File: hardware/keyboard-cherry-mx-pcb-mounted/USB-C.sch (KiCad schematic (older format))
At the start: 3 parts

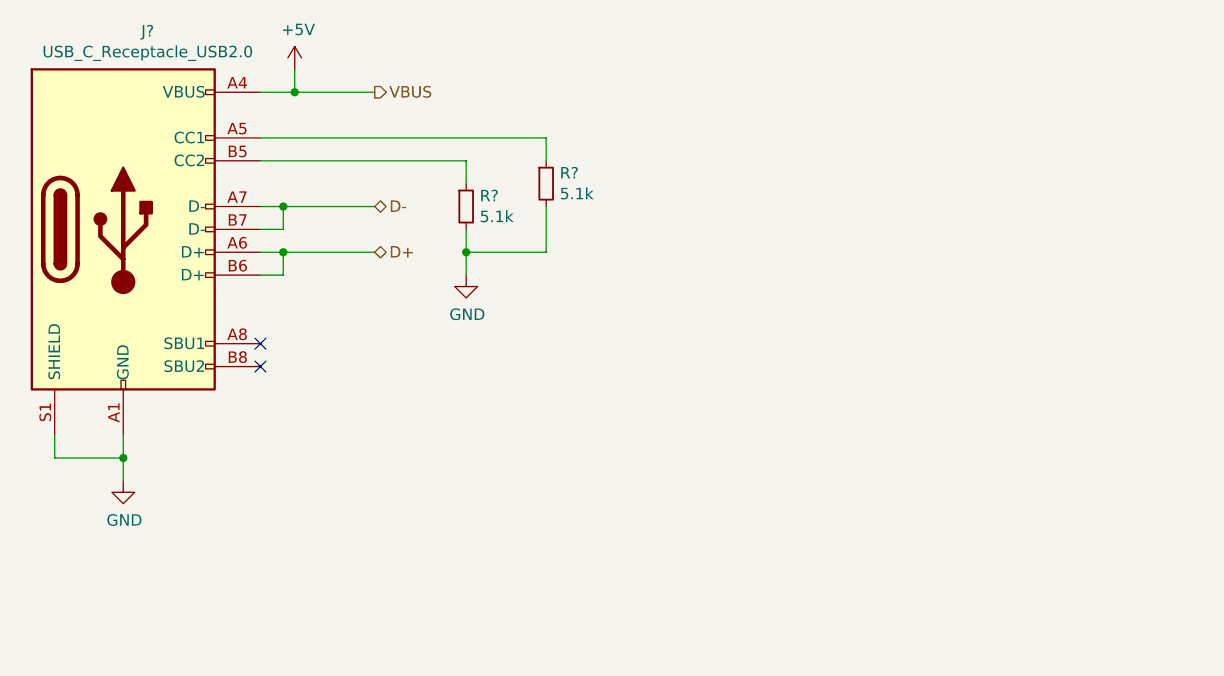
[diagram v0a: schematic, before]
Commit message: Adds completed sensor and power connections. Still need to add USB footprint then sch are done for version 1.0
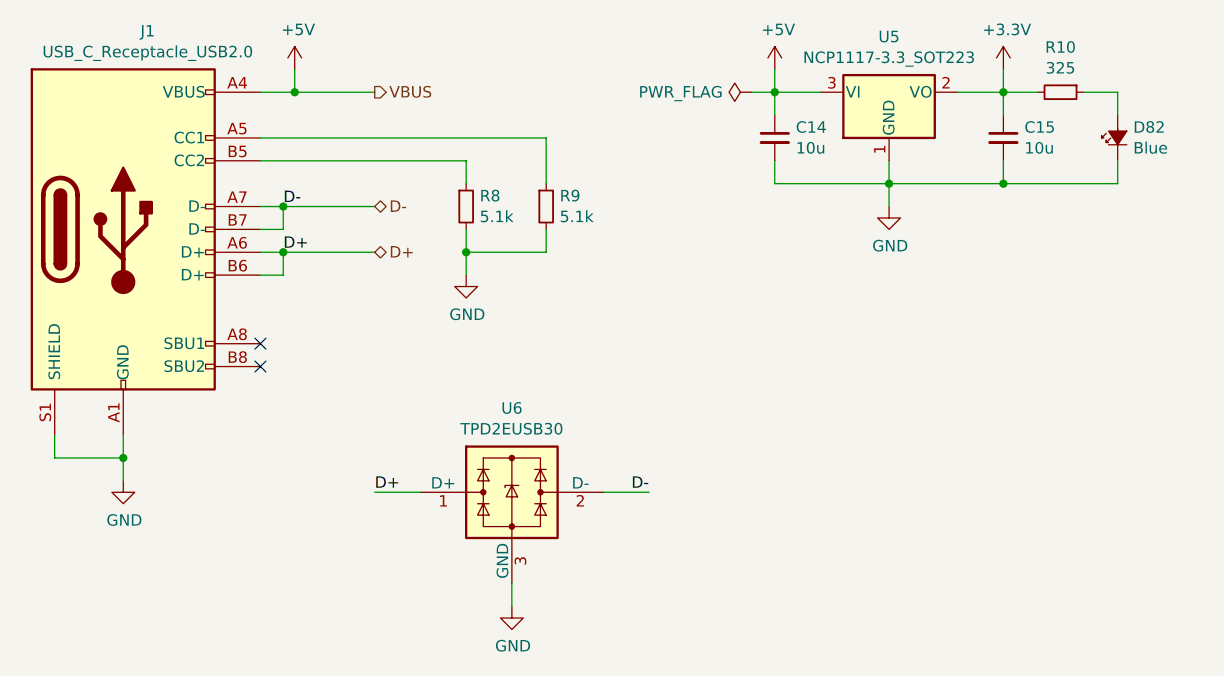
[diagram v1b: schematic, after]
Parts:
- added C14, C15: 10u, Capacitor_SMD:C_0805_2012Metric, symbol Device:C_Small
- added D82: Blue, symbol Device:LED_Small_ALT
- added R10: 325, symbol Device:R_Small
- added U5: NCP1117-3.3_SOT223, Package_TO_SOT_SMD:SOT-223-3_TabPin2, symbol Regulator_Linear:NCP1117-3.3_SOT223
- added U6: TPD2EUSB30, Package_TO_SOT_SMD:Texas_DRT-3, symbol Power_Protection:TPD2EUSB30
- gave numbers to parts that had none: 3
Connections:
- net +5V: now also C14.1, U5.3 (VI)
- net D+: now also U6.1 (D+)
- net D-: now also U6.2 (D-)
- net GND: now also C14.2, C15.2, D82.1 (K), U5.1 (GND), U6.3 (GND)
- new net: D82.2 (A), R10.1
- new net +3V3: C15.1, R10.2, U5.2 (VO)
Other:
- moved on the sheet: R9
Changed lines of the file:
@@
 $EndDescr
 $Comp
-L Connector:USB_C_Receptacle_USB2.0 J?
+L Connector:USB_C_Receptacle_USB2.0 J1
 U 1 1 5E8055B4
 P 2400 3250
-F 0 "J?" H 2507 4117 50  0000 C CNN
+F 0 "J1" H 2507 4117 50  0000 C CNN
 F 1 "USB_C_Receptacle_USB2.0" H 2507 4026 50  0000 C CNN
 F 2 "" H 2550 3250 50  0001 C CNN
@@
 D+
 $Comp
-L Device:R_Small R?
+L Device:R_Small R9
 U 1 1 5E80893D
-P 4250 3050
-F 0 "R?" H 4309 3096 50  0000 L CNN
-F 1 "5.1k" H 4309 3005 50  0000 L CNN
-F 2 "Resistor_SMD:R_0805_2012Metric" H 4250 3050 50  0001 C CNN
-F 3 "~" H 4250 3050 50  0001 C CNN
-	1    4250 3050
-	1    0    0    -1
-$EndComp
-$Comp
-L Device:R_Small R?
+P 4250 3150
+F 0 "R9" H 4309 3196 50  0000 L CNN
+F 1 "5.1k" H 4309 3105 50  0000 L CNN
+F 2 "Resistor_SMD:R_0805_2012Metric" H 4250 3150 50  0001 C CNN
+F 3 "~" H 4250 3150 50  0001 C CNN
+	1    4250 3150
+	1    0    0    -1
+$EndComp
+$Comp
+L Device:R_Small R8
 U 1 1 5E80B2F7
 P 3900 3150
-F 0 "R?" H 3959 3196 50  0000 L CNN
+F 0 "R8" H 3959 3196 50  0000 L CNN
 F 1 "5.1k" H 3959 3105 50  0000 L CNN
 F 2 "Resistor_SMD:R_0805_2012Metric" H 3900 3150 50  0001 C CNN
@@
 	3000 2850 4250 2850
 Wire Wire Line
-	4250 2850 4250 2950
-$Comp
-L power:GND #PWR?
+	4250 2850 4250 3050
+$Comp
+L power:GND #PWR023
 U 1 1 5E80BFE4
 P 3900 3450
-F 0 "#PWR?" H 3900 3200 50  0001 C CNN
+F 0 "#PWR023" H 3900 3200 50  0001 C CNN
 F 1 "GND" H 3905 3277 50  0000 C CNN
 F 2 "" H 3900 3450 50  0001 C CNN
@@
 Connection ~ 3900 3350
 Wire Wire Line
-	4250 3150 4250 3350
+	4250 3250 4250 3350
 Wire Wire Line
 	3900 3250 3900 3350
 $Comp
-L power:GND #PWR?
+L power:GND #PWR021
 U 1 1 5E80F482
 P 2400 4350
-F 0 "#PWR?" H 2400 4100 50  0001 C CNN
+F 0 "#PWR021" H 2400 4100 50  0001 C CNN
 F 1 "GND" H 2405 4177 50  0000 C CNN
 F 2 "" H 2400 4350 50  0001 C CNN
@@
 	2400 4250 2400 4150
 $Comp
-L power:+5V #PWR?
+L power:+5V #PWR022
 U 1 1 5E810FCD
 P 3150 2550
-F 0 "#PWR?" H 3150 2400 50  0001 C CNN
+F 0 "#PWR022" H 3150 2400 50  0001 C CNN
 F 1 "+5V" H 3165 2723 50  0000 C CNN
 F 2 "" H 3150 2550 50  0001 C CNN
@@
 NoConn ~ 3000 3750
 NoConn ~ 3000 3850
+$Comp
+L Regulator_Linear:NCP1117-3.3_SOT223 U5
+U 1 1 5EA493A5
+P 5750 2650
+F 0 "U5" H 5750 2892 50  0000 C CNN
+F 1 "NCP1117-3.3_SOT223" H 5750 2801 50  0000 C CNN
+F 2 "Package_TO_SOT_SMD:SOT-223-3_TabPin2" H 5750 2850 50  0001 C CNN
+F 3 "http://www.onsemi.com/pub_link/Collateral/NCP1117-D.PDF" H 5850 2400 50  0001 C CNN
+	1    5750 2650
+	1    0    0    -1
+$EndComp
+$Comp
+L Device:C_Small C15
+U 1 1 5EA4AE93
+P 6250 2850
+F 0 "C15" H 6342 2896 50  0000 L CNN
+F 1 "10u" H 6342 2805 50  0000 L CNN
+F 2 "Capacitor_SMD:C_0805_2012Metric" H 6250 2850 50  0001 C CNN
+F 3 "~" H 6250 2850 50  0001 C CNN
+	1    6250 2850
+	1    0    0    -1
+$EndComp
+$Comp
+L Device:C_Small C14
+U 1 1 5EA4B77C
+P 5250 2850
+F 0 "C14" H 5342 2896 50  0000 L CNN
+F 1 "10u" H 5342 2805 50  0000 L CNN
+F 2 "Capacitor_SMD:C_0805_2012Metric" H 5250 2850 50  0001 C CNN
+F 3 "~" H 5250 2850 50  0001 C CNN
+	1    5250 2850
+	1    0    0    -1
+$EndComp
+Wire Wire Line
+	6250 2650 6250 2750
+Wire Wire Line
+	6250 2950 6250 3050
+Wire Wire Line
+	5250 3050 5250 2950
+Wire Wire Line
+	5750 2950 5750 3050
+Connection ~ 5750 3050
+$Comp
+L power:GND #PWR0101
+U 1 1 5EA4DBB7
+P 5750 3150
+F 0 "#PWR0101" H 5750 2900 50  0001 C CNN
+F 1 "GND" H 5755 2977 50  0000 C CNN
+F 2 "" H 5750 3150 50  0001 C CNN
+F 3 "" H 5750 3150 50  0001 C CNN
+	1    5750 3150
+	1    0    0    -1
+$EndComp
+Wire Wire Line
+	5750 3150 5750 3050
+Wire Wire Line
+	5250 2550 5250 2650
+Wire Wire Line
+	5250 2650 5450 2650
+Connection ~ 5250 2650
+Wire Wire Line
+	5250 2650 5250 2750
+Wire Wire Line
+	5250 3050 5750 3050
+Wire Wire Line
+	5750 3050 6250 3050
+$Comp
+L power:+3.3V #PWR0103
+U 1 1 5EA55914
+P 6250 2550
+F 0 "#PWR0103" H 6250 2400 50  0001 C CNN
+F 1 "+3.3V" H 6265 2723 50  0000 C CNN
+F 2 "" H 6250 2550 50  0001 C CNN
+F 3 "" H 6250 2550 50  0001 C CNN
+	1    6250 2550
+	1    0    0    -1
+$EndComp
+Wire Wire Line
+	6250 2550 6250 2650
+Connection ~ 6250 2650
+$Comp
+L Device:R_Small R10
+U 1 1 5EA56F50
+P 6500 2650
+F 0 "R10" V 6304 2650 50  0000 C CNN
+F 1 "325" V 6395 2650 50  0000 C CNN
+F 2 "" H 6500 2650 50  0001 C CNN
+F 3 "~" H 6500 2650 50  0001 C CNN
+	1    6500 2650
+	0    1    1    0
+$EndComp
+$Comp
+L Device:LED_Small_ALT D82
+U 1 1 5EA59D3F
+P 6750 2850
+F 0 "D82" V 6796 2782 50  0000 R CNN
+F 1 "Blue" V 6705 2782 50  0000 R CNN
+F 2 "" V 6750 2850 50  0001 C CNN
+F 3 "~" V 6750 2850 50  0001 C CNN
+F 4 "APTD2012LQBC/D" V 6750 2850 50  0001 C CNN "P/N"
+F 5 "2.65V" V 6750 2850 50  0001 C CNN "Vf"
+F 6 "2mA" V 6750 2850 50  0001 C CNN "If"
+	1    6750 2850
+	0    -1   -1   0
+$EndComp
+Wire Wire Line
+	6400 2650 6250 2650
+Wire Wire Line
+	6250 3050 6750 3050
+Wire Wire Line
+	6750 3050 6750 2950
+Connection ~ 6250 3050
+Wire Wire Line
+	6750 2750 6750 2650
+Wire Wire Line
+	6750 2650 6600 2650
+Wire Wire Line
+	6050 2650 6250 2650
+$Comp
+L power:+5V #PWR0102
+U 1 1 5EB4F139
+P 5250 2550
+F 0 "#PWR0102" H 5250 2400 50  0001 C CNN
+F 1 "+5V" H 5265 2723 50  0000 C CNN
+F 2 "" H 5250 2550 50  0001 C CNN
+F 3 "" H 5250 2550 50  0001 C CNN
+	1    5250 2550
+	1    0    0    -1
+$EndComp
+$Comp
+L power:PWR_FLAG #FLG0101
+U 1 1 5EB50AC0
+P 5150 2650
+F 0 "#FLG0101" H 5150 2725 50  0001 C CNN
+F 1 "PWR_FLAG" V 5150 2777 50  0000 L CNN
+F 2 "" H 5150 2650 50  0001 C CNN
+F 3 "~" H 5150 2650 50  0001 C CNN
+	1    5150 2650
+	0    -1   -1   0
+$EndComp
+Wire Wire Line
+	5150 2650 5250 2650
+$Comp
+L Power_Protection:TPD2EUSB30 U6
+U 1 1 5EB6D136
+P 4100 4400
+F 0 "U6" H 4100 4767 50  0000 C CNN
+F 1 "TPD2EUSB30" H 4100 4676 50  0000 C CNN
+F 2 "Package_TO_SOT_SMD:Texas_DRT-3" H 3350 4100 50  0001 C CNN
+F 3 "http://www.ti.com/lit/ds/symlink/tpd2eusb30a.pdf" H 4100 4400 50  0001 C CNN
+	1    4100 4400
+	1    0    0    -1
+$EndComp
+Text Label 3100 3150 0    50   ~ 0
+D-
+Text Label 3100 3350 0    50   ~ 0
+D+
+$Comp
+L power:GND #PWR024
+U 1 1 5EB72B3A
+P 4100 4900
+F 0 "#PWR024" H 4100 4650 50  0001 C CNN
+F 1 "GND" H 4105 4727 50  0000 C CNN
+F 2 "" H 4100 4900 50  0001 C CNN
+F 3 "" H 4100 4900 50  0001 C CNN
+	1    4100 4900
+	1    0    0    -1
+$EndComp
+Wire Wire Line
+	4100 4900 4100 4800
+Text Label 4700 4400 2    50   ~ 0
+D-
+Wire Wire Line
+	4700 4400 4500 4400
+Wire Wire Line
+	3700 4400 3500 4400
+Text Label 3500 4400 0    50   ~ 0
+D+
 $EndSCHEMATC

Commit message: All keys except for function key row are laid out to their exact locations.
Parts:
- D82: footprint (none) -> LED_SMD:LED_0805_2012Metric
- J1: footprint (none) -> Sij_Connectors:USB_C_Receptacle_Wurth_632723100021; P/N (none) -> 632723100021
- R10: footprint (none) -> Resistor_SMD:R_0805_2012Metric
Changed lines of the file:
@@
 F 0 "J1" H 2507 4117 50  0000 C CNN
 F 1 "USB_C_Receptacle_USB2.0" H 2507 4026 50  0000 C CNN
-F 2 "" H 2550 3250 50  0001 C CNN
+F 2 "Sij_Connectors:USB_C_Receptacle_Wurth_632723100021" H 2550 3250 50  0001 C CNN
 F 3 "https://www.usb.org/sites/default/files/documents/usb_type-c.zip" H 2550 3250 50  0001 C CNN
+F 4 "632723100021" H 2400 3250 50  0001 C CNN "P/N"
 	1    2400 3250
 	1    0    0    -1
@@
 F 0 "R10" V 6304 2650 50  0000 C CNN
 F 1 "325" V 6395 2650 50  0000 C CNN
-F 2 "" H 6500 2650 50  0001 C CNN
+F 2 "Resistor_SMD:R_0805_2012Metric" H 6500 2650 50  0001 C CNN
 F 3 "~" H 6500 2650 50  0001 C CNN
 	1    6500 2650
@@
 F 0 "D82" V 6796 2782 50  0000 R CNN
 F 1 "Blue" V 6705 2782 50  0000 R CNN
-F 2 "" V 6750 2850 50  0001 C CNN
+F 2 "LED_SMD:LED_0805_2012Metric" V 6750 2850 50  0001 C CNN
 F 3 "~" V 6750 2850 50  0001 C CNN
 F 4 "APTD2012LQBC/D" V 6750 2850 50  0001 C CNN "P/N"

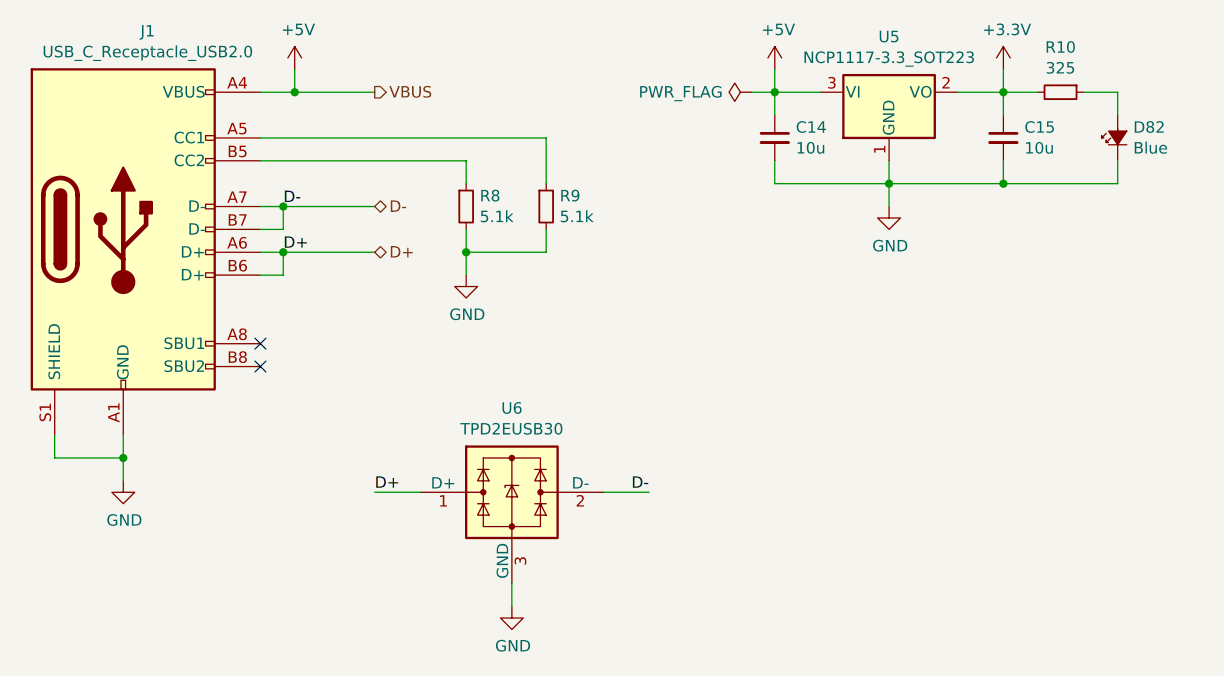
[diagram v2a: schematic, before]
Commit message: Aligns the keys so the column connections are more consistent. e.g. right most keys will have same column connection.
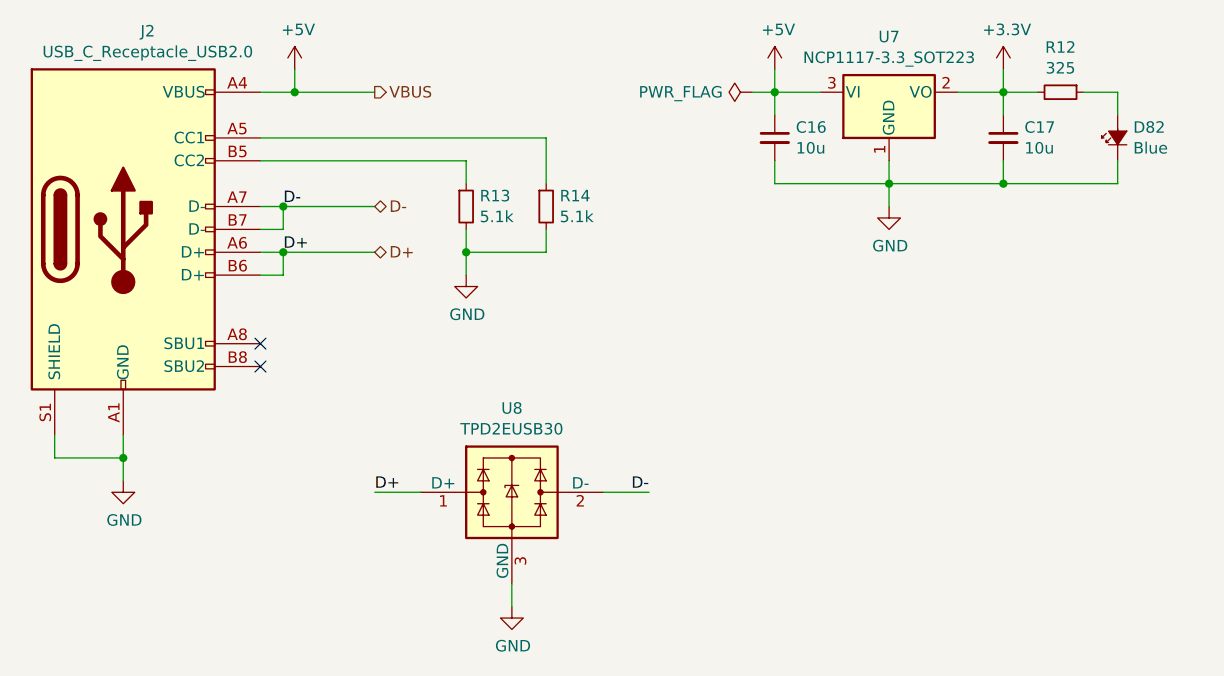
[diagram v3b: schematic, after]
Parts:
- renumbered C14 to C16, C15 to C17, J1 to J2, R10 to R12, R8 to R13, R9 to R14, U5 to U7, U6 to U8
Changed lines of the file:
@@
 $EndDescr
 $Comp
-L Connector:USB_C_Receptacle_USB2.0 J1
+L Connector:USB_C_Receptacle_USB2.0 J2
 U 1 1 5E8055B4
 P 2400 3250
-F 0 "J1" H 2507 4117 50  0000 C CNN
+F 0 "J2" H 2507 4117 50  0000 C CNN
 F 1 "USB_C_Receptacle_USB2.0" H 2507 4026 50  0000 C CNN
 F 2 "Sij_Connectors:USB_C_Receptacle_Wurth_632723100021" H 2550 3250 50  0001 C CNN
@@
 D+
 $Comp
-L Device:R_Small R9
+L Device:R_Small R14
 U 1 1 5E80893D
 P 4250 3150
-F 0 "R9" H 4309 3196 50  0000 L CNN
+F 0 "R14" H 4309 3196 50  0000 L CNN
 F 1 "5.1k" H 4309 3105 50  0000 L CNN
 F 2 "Resistor_SMD:R_0805_2012Metric" H 4250 3150 50  0001 C CNN
@@
 $EndComp
 $Comp
-L Device:R_Small R8
+L Device:R_Small R13
 U 1 1 5E80B2F7
 P 3900 3150
-F 0 "R8" H 3959 3196 50  0000 L CNN
+F 0 "R13" H 3959 3196 50  0000 L CNN
 F 1 "5.1k" H 3959 3105 50  0000 L CNN
 F 2 "Resistor_SMD:R_0805_2012Metric" H 3900 3150 50  0001 C CNN
@@
 	4250 2850 4250 3050
 $Comp
-L power:GND #PWR023
+L power:GND #PWR033
 U 1 1 5E80BFE4
 P 3900 3450
-F 0 "#PWR023" H 3900 3200 50  0001 C CNN
+F 0 "#PWR033" H 3900 3200 50  0001 C CNN
 F 1 "GND" H 3905 3277 50  0000 C CNN
 F 2 "" H 3900 3450 50  0001 C CNN
@@
 	3900 3250 3900 3350
 $Comp
-L power:GND #PWR021
+L power:GND #PWR034
 U 1 1 5E80F482
 P 2400 4350
-F 0 "#PWR021" H 2400 4100 50  0001 C CNN
+F 0 "#PWR034" H 2400 4100 50  0001 C CNN
 F 1 "GND" H 2405 4177 50  0000 C CNN
 F 2 "" H 2400 4350 50  0001 C CNN
@@
 	2400 4250 2400 4150
 $Comp
-L power:+5V #PWR022
+L power:+5V #PWR029
 U 1 1 5E810FCD
 P 3150 2550
-F 0 "#PWR022" H 3150 2400 50  0001 C CNN
+F 0 "#PWR029" H 3150 2400 50  0001 C CNN
 F 1 "+5V" H 3165 2723 50  0000 C CNN
 F 2 "" H 3150 2550 50  0001 C CNN
@@
 NoConn ~ 3000 3850
 $Comp
-L Regulator_Linear:NCP1117-3.3_SOT223 U5
+L Regulator_Linear:NCP1117-3.3_SOT223 U7
 U 1 1 5EA493A5
 P 5750 2650
-F 0 "U5" H 5750 2892 50  0000 C CNN
+F 0 "U7" H 5750 2892 50  0000 C CNN
 F 1 "NCP1117-3.3_SOT223" H 5750 2801 50  0000 C CNN
 F 2 "Package_TO_SOT_SMD:SOT-223-3_TabPin2" H 5750 2850 50  0001 C CNN
@@
 $EndComp
 $Comp
-L Device:C_Small C15
+L Device:C_Small C17
 U 1 1 5EA4AE93
 P 6250 2850
-F 0 "C15" H 6342 2896 50  0000 L CNN
+F 0 "C17" H 6342 2896 50  0000 L CNN
 F 1 "10u" H 6342 2805 50  0000 L CNN
 F 2 "Capacitor_SMD:C_0805_2012Metric" H 6250 2850 50  0001 C CNN
@@
 $EndComp
 $Comp
-L Device:C_Small C14
+L Device:C_Small C16
 U 1 1 5EA4B77C
 P 5250 2850
-F 0 "C14" H 5342 2896 50  0000 L CNN
+F 0 "C16" H 5342 2896 50  0000 L CNN
 F 1 "10u" H 5342 2805 50  0000 L CNN
 F 2 "Capacitor_SMD:C_0805_2012Metric" H 5250 2850 50  0001 C CNN
@@
 Connection ~ 5750 3050
 $Comp
-L power:GND #PWR0101
+L power:GND #PWR032
 U 1 1 5EA4DBB7
 P 5750 3150
-F 0 "#PWR0101" H 5750 2900 50  0001 C CNN
+F 0 "#PWR032" H 5750 2900 50  0001 C CNN
 F 1 "GND" H 5755 2977 50  0000 C CNN
 F 2 "" H 5750 3150 50  0001 C CNN
@@
 	5750 3050 6250 3050
 $Comp
-L power:+3.3V #PWR0103
+L power:+3.3V #PWR031
 U 1 1 5EA55914
 P 6250 2550
-F 0 "#PWR0103" H 6250 2400 50  0001 C CNN
+F 0 "#PWR031" H 6250 2400 50  0001 C CNN
 F 1 "+3.3V" H 6265 2723 50  0000 C CNN
 F 2 "" H 6250 2550 50  0001 C CNN
@@
 Connection ~ 6250 2650
 $Comp
-L Device:R_Small R10
+L Device:R_Small R12
 U 1 1 5EA56F50
 P 6500 2650
-F 0 "R10" V 6304 2650 50  0000 C CNN
+F 0 "R12" V 6304 2650 50  0000 C CNN
 F 1 "325" V 6395 2650 50  0000 C CNN
 F 2 "Resistor_SMD:R_0805_2012Metric" H 6500 2650 50  0001 C CNN
@@
 	6050 2650 6250 2650
 $Comp
-L power:+5V #PWR0102
+L power:+5V #PWR030
 U 1 1 5EB4F139
 P 5250 2550
-F 0 "#PWR0102" H 5250 2400 50  0001 C CNN
+F 0 "#PWR030" H 5250 2400 50  0001 C CNN
 F 1 "+5V" H 5265 2723 50  0000 C CNN
 F 2 "" H 5250 2550 50  0001 C CNN
@@
 $EndComp
 $Comp
-L power:PWR_FLAG #FLG0101
+L power:PWR_FLAG #FLG05
 U 1 1 5EB50AC0
 P 5150 2650
-F 0 "#FLG0101" H 5150 2725 50  0001 C CNN
+F 0 "#FLG05" H 5150 2725 50  0001 C CNN
 F 1 "PWR_FLAG" V 5150 2777 50  0000 L CNN
 F 2 "" H 5150 2650 50  0001 C CNN
@@
 	5150 2650 5250 2650
 $Comp
-L Power_Protection:TPD2EUSB30 U6
+L Power_Protection:TPD2EUSB30 U8
 U 1 1 5EB6D136
 P 4100 4400
-F 0 "U6" H 4100 4767 50  0000 C CNN
+F 0 "U8" H 4100 4767 50  0000 C CNN
 F 1 "TPD2EUSB30" H 4100 4676 50  0000 C CNN
 F 2 "Package_TO_SOT_SMD:Texas_DRT-3" H 3350 4100 50  0001 C CNN
@@
 D+
 $Comp
-L power:GND #PWR024
+L power:GND #PWR035
 U 1 1 5EB72B3A
 P 4100 4900
-F 0 "#PWR024" H 4100 4650 50  0001 C CNN
+F 0 "#PWR035" H 4100 4650 50  0001 C CNN
 F 1 "GND" H 4105 4727 50  0000 C CNN
 F 2 "" H 4100 4900 50  0001 C CNN

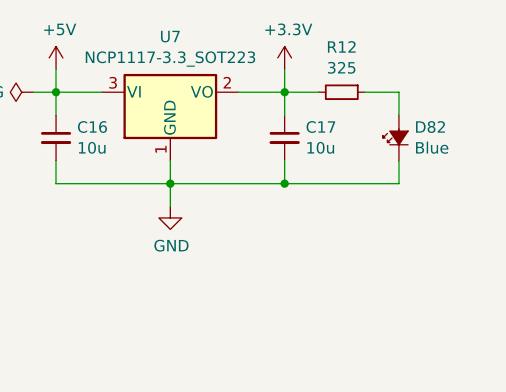
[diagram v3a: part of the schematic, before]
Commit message: Changes LED for power to orange on cherry mx pcb mounted keyboard.
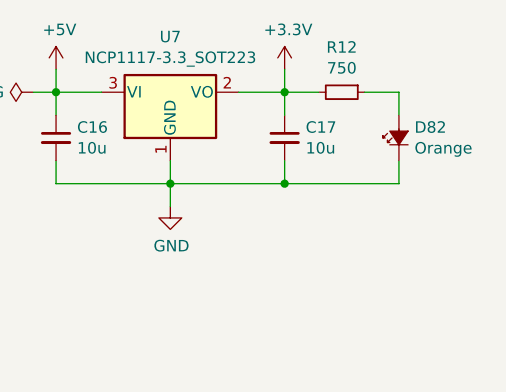
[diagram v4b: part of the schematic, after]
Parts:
- D82: value Blue -> Orange; P/N APTD2012LQBC/D -> APT2012LSECK/J4-PRV; Vf 2.65V -> 1.8V
- R12: value 325 -> 750
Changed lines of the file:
@@
 P 6500 2650
 F 0 "R12" V 6304 2650 50  0000 C CNN
-F 1 "325" V 6395 2650 50  0000 C CNN
+F 1 "750" V 6395 2650 50  0000 C CNN
 F 2 "Resistor_SMD:R_0805_2012Metric" H 6500 2650 50  0001 C CNN
 F 3 "~" H 6500 2650 50  0001 C CNN
@@
 P 6750 2850
 F 0 "D82" V 6796 2782 50  0000 R CNN
-F 1 "Blue" V 6705 2782 50  0000 R CNN
+F 1 "Orange" V 6705 2782 50  0000 R CNN
 F 2 "LED_SMD:LED_0805_2012Metric" V 6750 2850 50  0001 C CNN
 F 3 "~" V 6750 2850 50  0001 C CNN
-F 4 "APTD2012LQBC/D" V 6750 2850 50  0001 C CNN "P/N"
-F 5 "2.65V" V 6750 2850 50  0001 C CNN "Vf"
+F 4 "APT2012LSECK/J4-PRV" V 6750 2850 50  0001 C CNN "P/N"
+F 5 "1.8V" V 6750 2850 50  0001 C CNN "Vf"
 F 6 "2mA" V 6750 2850 50  0001 C CNN "If"
 	1    6750 2850
